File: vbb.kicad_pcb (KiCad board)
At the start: 2 copper layers, 24 parts, among them CON1 BARREL_JACK, J1 Screw_Terminal_1x02, P1 CONN_02X01, P3 CONN_02X04, P4 USB_B, P5 USB_B, P6 USB_B, P7 USB_A

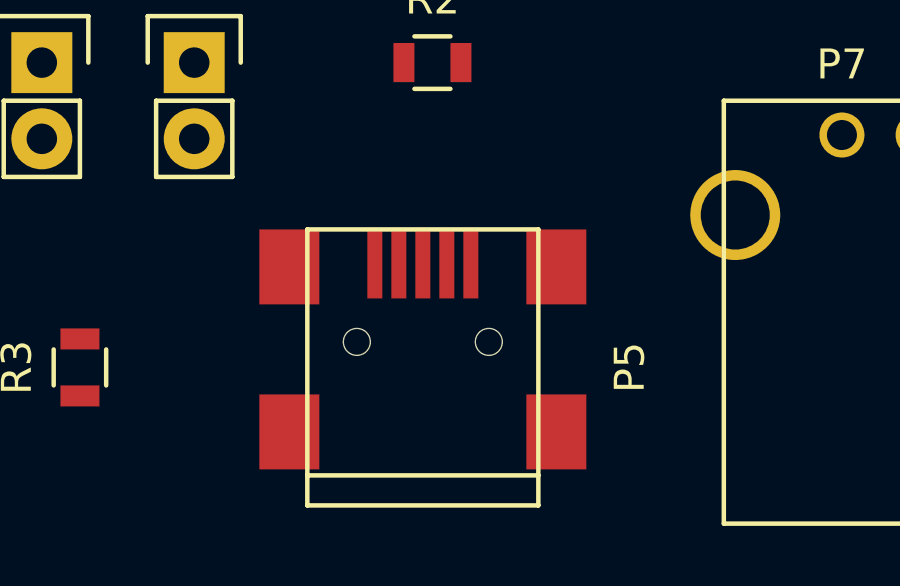
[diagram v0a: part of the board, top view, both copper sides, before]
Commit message: Replaced old surface mount USB Mini with through hole Omron Mini-USB B through hole XM7D-0512
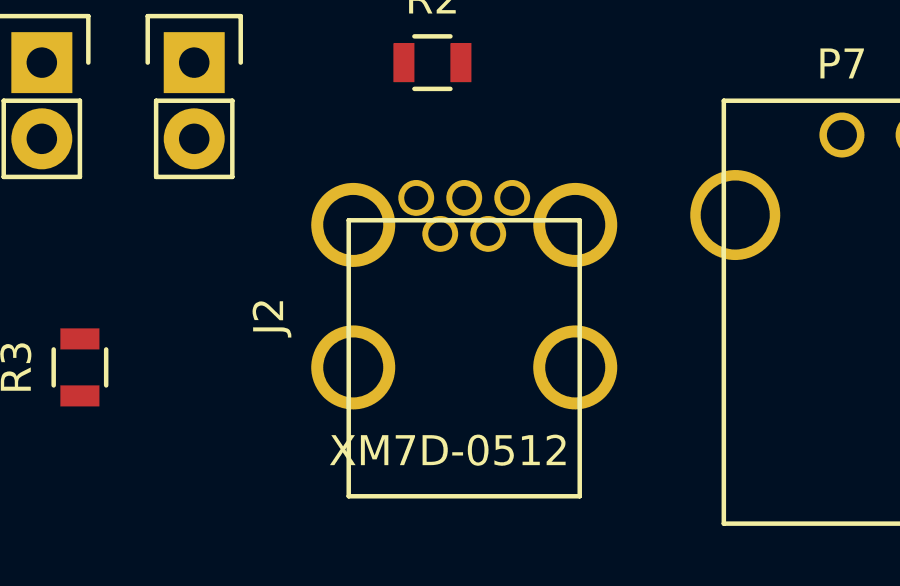
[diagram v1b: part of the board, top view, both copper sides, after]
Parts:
- removed P5: USB_B, Connect:USB_Mini-B
- added J2: XM7D-0512, Omron:XM7D-0512, F.Cu at (127.1, 116.1)

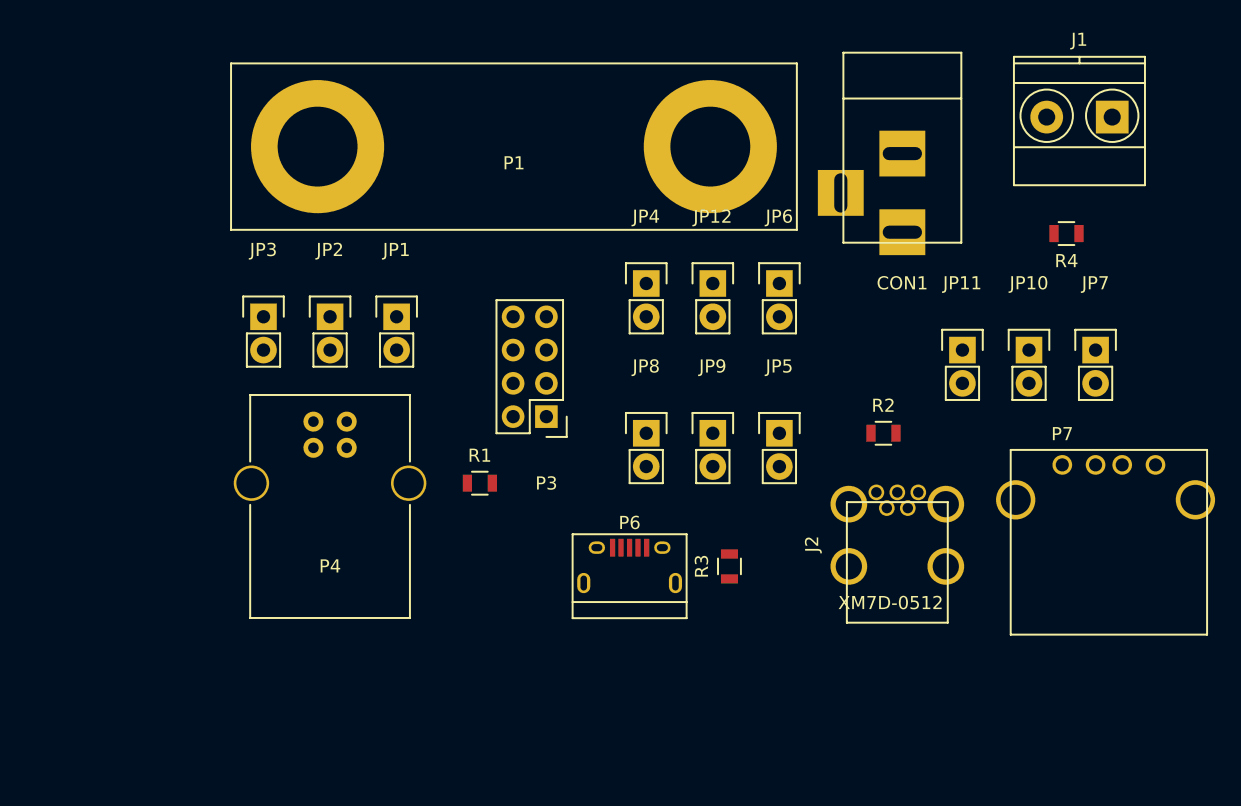
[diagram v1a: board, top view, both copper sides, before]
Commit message: Combined separate jumpers into a 2x03 connector As a result, board now fits the 50mmx50mm size group.
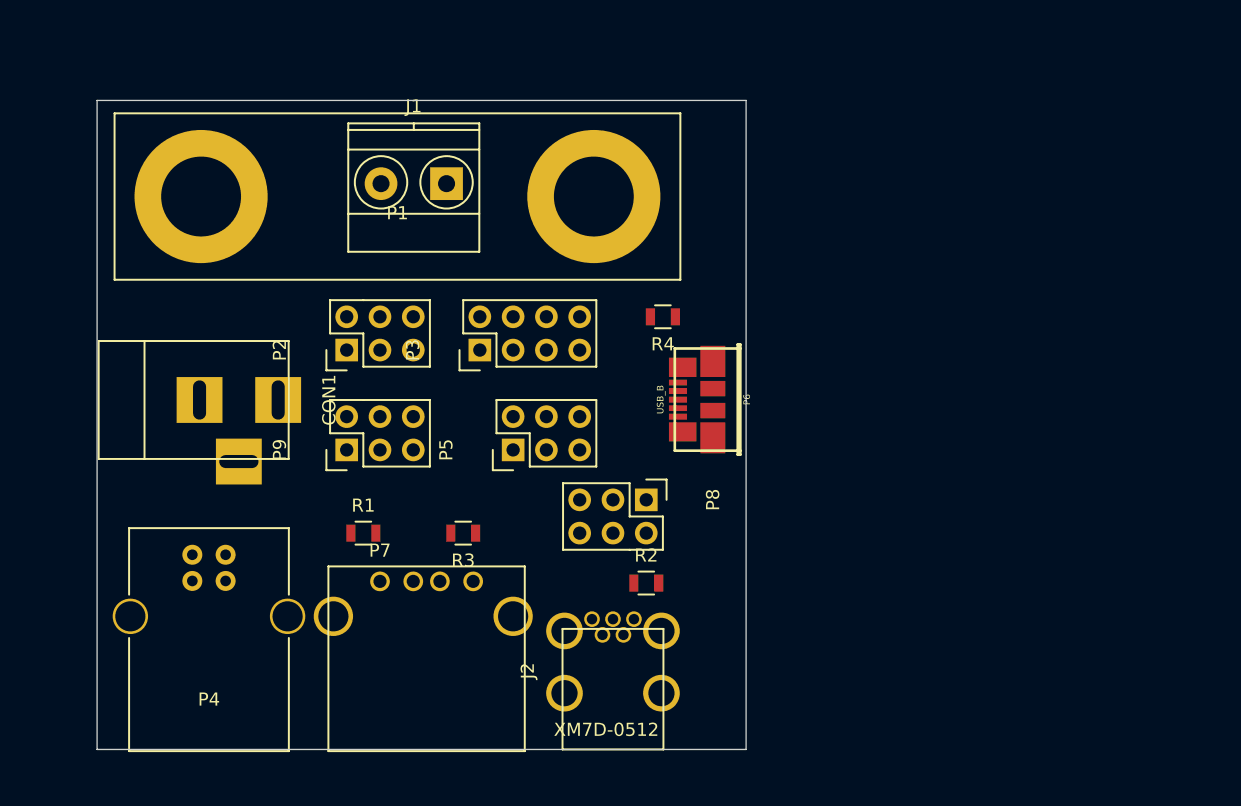
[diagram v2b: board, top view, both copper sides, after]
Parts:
- removed JP1, JP10, JP11, JP12, JP2, JP3, JP4, JP5, JP6, JP7, JP8, JP9: JUMPER_NO_Small, Pin_Headers:Pin_Header_Straight_1x02
- added P2: CONN_02X03, Pin_Headers:Pin_Header_Straight_2x03, F.Cu at (85.1, 95.2)
- added P5: CONN_02X03, Pin_Headers:Pin_Header_Straight_2x03, F.Cu at (97.8, 102.9)
- added P8: CONN_02X03, Pin_Headers:Pin_Header_Straight_2x03, F.Cu at (108.0, 106.7)
- added P9: CONN_02X03, Pin_Headers:Pin_Header_Straight_2x03, F.Cu at (85.1, 102.9)
- P6: footprint Connect:USB_Micro-B -> w_conn_pc:conn_usb_B_micro_smd
- moved CON1 57.1 mm to (73.7, 99.1), turned to 0 degrees
- moved P7 52.8 mm to (87.6, 112.9)
- moved J1 51.1 mm to (92.7, 82.5)
- moved R4 31.4 mm to (109.2, 92.7)
- moved J2 23.8 mm to (105.4, 125.7)
- moved R2 21.4 mm to (108.0, 113.0)
- moved R3 20.5 mm to (94.0, 109.2), turned to 180 degrees
- moved P6 14.3 mm to (113.0, 99.0), turned to 90 degrees
- moved P4 13.7 mm to (75.8, 110.9)
- moved P1 9.67 mm to (89.0, 83.5)
- moved R1 9.67 mm to (86.4, 109.2)
- moved P3 7.18 mm to (95.2, 95.2), turned to 90 degrees
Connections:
- P1 pad 2: /GND -> Net-(P1-Pad2)
- P3 pad 1: /GND -> Net-(P1-Pad2)
- P3 pad 3: /GND -> Net-(P1-Pad2)
- P3 pad 5: /GND -> Net-(P1-Pad2)
- P3 pad 7: /GND -> Net-(P1-Pad2)
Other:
- board outline added: 49.5 x 49.5 mm

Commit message: First pass through TopoR
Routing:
- net /GND: track 0.00 -> 112.6 mm
- net /VCC: track 0.00 -> 82.2 mm
- net Net-(P7-Pad5): track 0.00 -> 44.6 mm
- net Net-(P2-Pad3): track 0.00 -> 28.6 mm
- net Net-(J2-Pad2): track 0.00 -> 28.2 mm
- net Net-(P2-Pad6): track 0.00 -> 26.9 mm
- net Net-(P2-Pad5): track 0.00 -> 25.2 mm
- net Net-(P6-Pad5): track 0.00 -> 25.0 mm
- net Net-(P2-Pad2): track 0.00 -> 24.1 mm
- net Net-(P2-Pad4): track 0.00 -> 23.6 mm
- net Net-(P4-Pad5): track 0.00 -> 21.3 mm
- net Net-(J2-Pad0): track 0.00 -> 20.6 mm
- net Net-(P1-Pad2): track 0.00 -> 19.7 mm
- net Net-(J2-Pad3): track 0.00 -> 16.9 mm
- net Net-(J2-Pad1): track 0.00 -> 16.8 mm
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
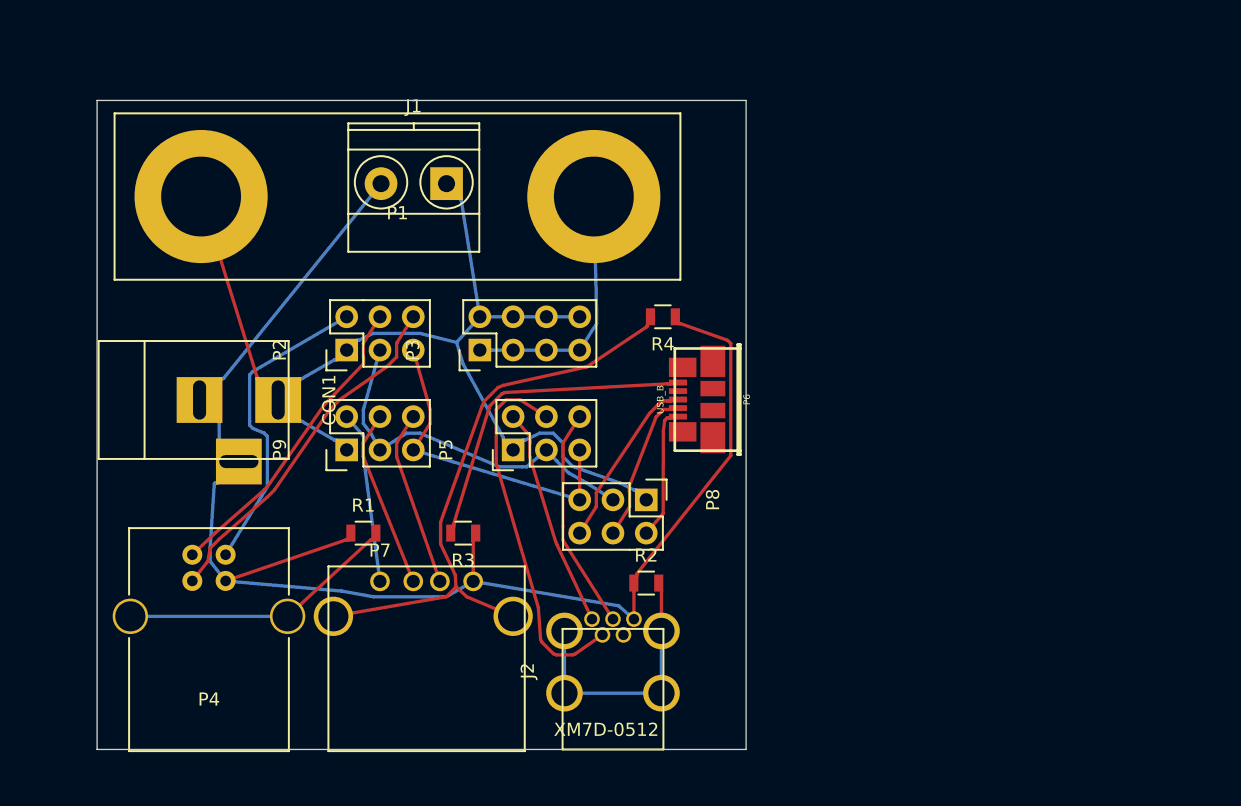
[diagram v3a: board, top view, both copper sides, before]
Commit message: Files should be ready: Copper pours on both sides Added jumpers for current measurement Added silkscreen text VCC/GNC tracks are twice as wide.
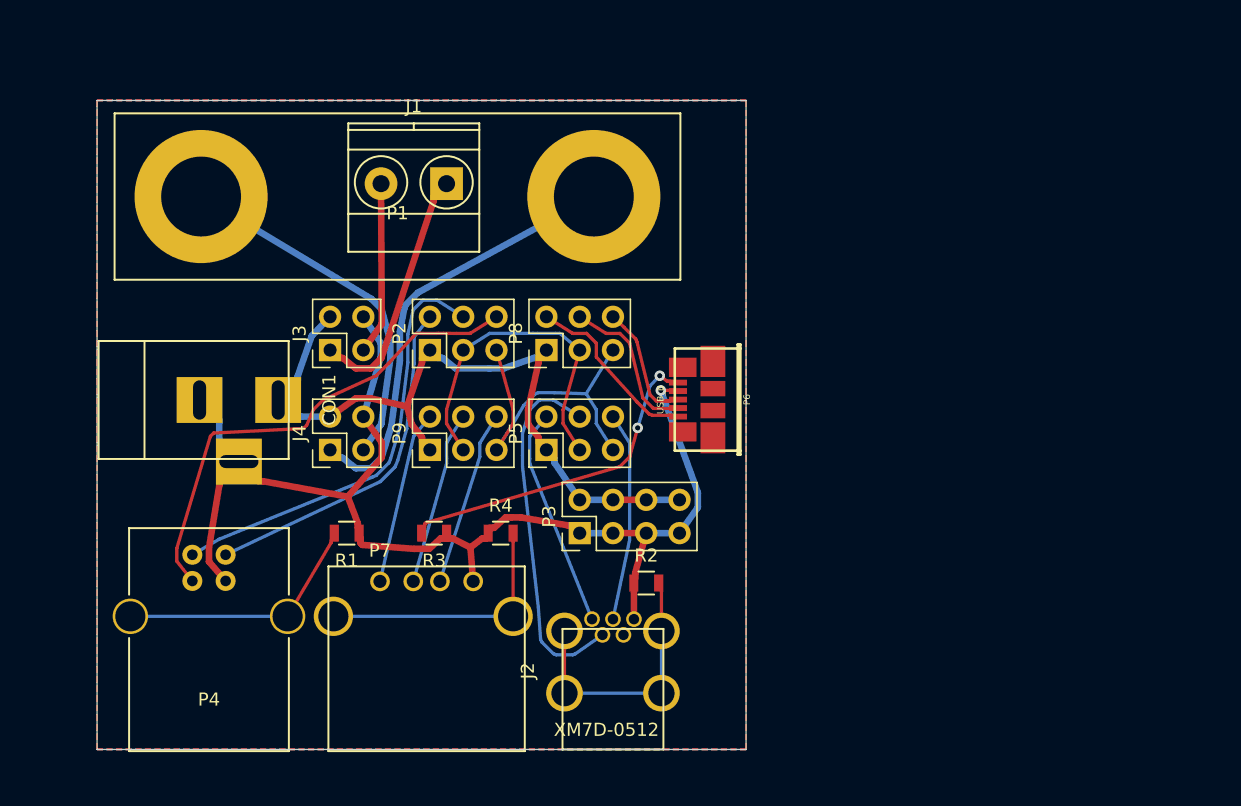
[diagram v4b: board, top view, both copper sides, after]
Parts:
- added J3: CONN_02X02, Pin_Headers:Pin_Header_Straight_2x02_Pitch2.54mm, F.Cu at (83.8, 95.2)
- added J4: CONN_02X02, Pin_Headers:Pin_Header_Straight_2x02_Pitch2.54mm, F.Cu at (83.8, 102.9)
- P2, P5, P8, P9: footprint Pin_Headers:Pin_Header_Straight_2x03 -> Pin_Headers:Pin_Header_Straight_2x03_Pitch2.54mm
- P3: footprint Pin_Headers:Pin_Header_Straight_2x04 -> Pin_Headers:Pin_Header_Straight_2x04_Pitch2.54mm
- moved R4 20.6 mm to (96.8, 109.2), turned to 0 degrees
- moved P3 15.9 mm to (102.9, 109.2)
- moved P8 13.7 mm to (100.3, 95.2), turned to 90 degrees
- moved P2 6.35 mm to (91.4, 95.2)
- moved P9 6.35 mm to (91.4, 102.9)
- moved P5 2.54 mm to (100.3, 102.9)
- moved R3 2.22 mm to (91.8, 109.2)
- moved R1 1.27 mm to (85.1, 109.2), turned to 180 degrees
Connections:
- J1 pad 1: /VCC -> /VCC2
- J1 pad 2: /GND -> /GND2
- P1 pad 1: /VCC -> /GND1
- P1 pad 2: Net-(P1-Pad2) -> /VCC1
- P3 pad 1: Net-(P1-Pad2) -> /GND
- P3 pad 3: Net-(P1-Pad2) -> /GND
- P3 pad 5: Net-(P1-Pad2) -> /GND
- P3 pad 7: Net-(P1-Pad2) -> /GND
- P6 pad 4: Net-(P6-Pad4) -> /GND
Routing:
- net /VCC1: track 0.00 -> 33.3 mm
- net /GND1: track 0.00 -> 27.6 mm
- net /VCC: track 82.2 -> 57.7 mm
- net Net-(P7-Pad5): track 44.6 -> 20.1 mm
- net Net-(P1-Pad2): track 19.7 -> 0.00 mm
- net /VCC2: track 0.00 -> 19.1 mm
- net /GND: track 112.6 -> 94.1 mm, vias 0 -> 1
- net /GND2: track 0.00 -> 13.1 mm
- net Net-(P2-Pad6): track 26.9 -> 37.1 mm
- net Net-(P2-Pad4): track 23.6 -> 33.0 mm
- net Net-(P6-Pad3): track 13.3 -> 9.17 mm
- net Net-(P6-Pad1): track 10.2 -> 13.7 mm
- net Net-(P2-Pad2): track 24.1 -> 26.7 mm
- net Net-(P2-Pad3): track 28.6 -> 26.0 mm
- net Net-(P4-Pad5): track 21.3 -> 19.3 mm
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- added copper zone on B.Cu, net /GND
- added copper zone on F.Cu, net /GND
- added copper zone on B.Cu, net /VCC
- added copper zone on F.Cu, net /VCC
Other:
- net class GND added: clearance 0.2, trace_width 0.5, via_dia 0.8, via_drill 0.4
- net class VCC added: clearance 0.2, trace_width 0.5, via_dia 0.8, via_drill 0.4
- board text added: "VCC Breakout Board"
- board text added: "© 2017 Udi Finkelstein https://github.com/udif/vbb"

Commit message: Fixes DRC by changing track-to-track clearance to 0.18mm and by deleting redundant multiple copper pours.
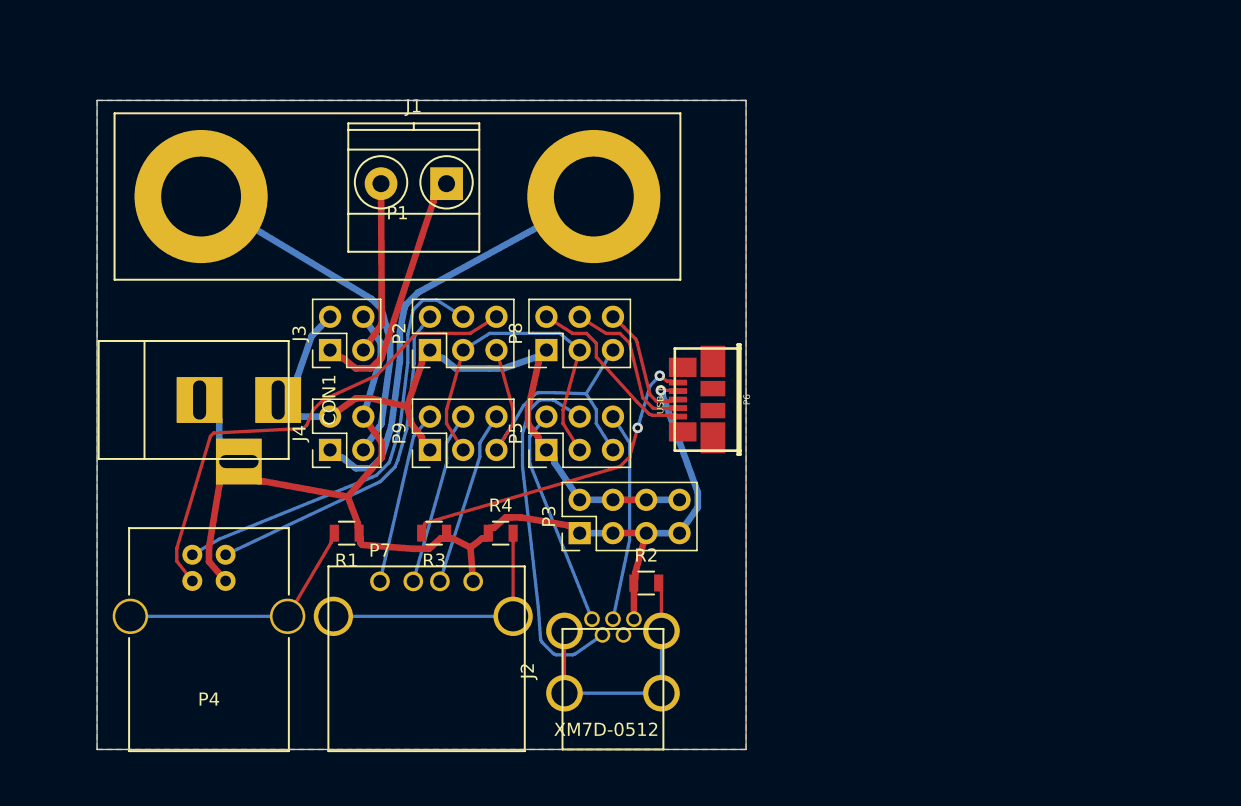
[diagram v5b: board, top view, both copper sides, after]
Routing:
- removed copper zone on B.Cu, net /GND
- removed copper zone on F.Cu, net /VCC
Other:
- net class Default: clearance 0.2 -> 0.18
- rule trace_clearance: 0.2 -> 0.18
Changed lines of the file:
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@@
   (layers
     (0 F.Cu signal)
-    (31 B.Cu signal hide)
+    (31 B.Cu signal)
     (32 B.Adhes user)
     (33 F.Adhes user)
@@
   (setup
     (last_trace_width 0.25)
-    (trace_clearance 0.2)
+    (trace_clearance 0.18)
     (zone_clearance 0.508)
     (zone_45_only no)
@@
     (pad_to_mask_clearance 0)
     (aux_axis_origin 0 0)
-    (visible_elements 7FFFFFFF)
+    (visible_elements 7FFFEFFF)
     (pcbplotparams
-      (layerselection 0x00030_ffffffff)
+      (layerselection 0x000fc_ffffffff)
       (usegerberextensions false)
       (excludeedgelayer true)
@@
   (net 25 /VCC1)
   (net_class Default "This is the default net class."
-    (clearance 0.2)
+    (clearance 0.18)
     (trace_width 0.25)
     (via_dia 0.8)
@@
   (segment (start 90.5271 90.8649) (end 89.5949 91.7971) (width 0.5) (layer B.Cu) (net 25))
   (segment (start 103.9498 83.534) (end 90.5271 90.8649) (width 0.5) (layer B.Cu) (net 25))
-  (zone (net 1) (net_name /GND) (layer B.Cu) (hatch edge 0.508)
-    (connect_pads (clearance 0.508))
-    (min_thickness 0.254)
-    (fill (arc_segments 16) (thermal_gap 0.508) (thermal_bridge_width 0.508))
-    (polygon
-      (pts
-        (xy 115.57 125.73) (xy 66.04 125.73) (xy 66.04 76.2) (xy 115.57 76.2)
-      )
-    )
-  )
-  (zone (net 1) (net_name /GND) (layer B.Cu) (hatch edge 0.508)
-    (connect_pads (clearance 0.508))
-    (min_thickness 0.254)
-    (fill (arc_segments 16) (thermal_gap 0.508) (thermal_bridge_width 0.508))
-    (polygon
-      (pts
-        (xy 66.04 76.2) (xy 115.57 76.2) (xy 115.57 125.73) (xy 66.04 125.73)
-      )
-    )
-  )
-  (zone (net 2) (net_name /VCC) (layer F.Cu) (hatch edge 0.508)
-    (connect_pads (clearance 0.508))
-    (min_thickness 0.254)
-    (fill (arc_segments 16) (thermal_gap 0.508) (thermal_bridge_width 0.508))
-    (polygon
-      (pts
-        (xy 66.04 76.2) (xy 115.57 76.2) (xy 115.57 125.73) (xy 66.04 125.73)
-      )
-    )
-  )
   (zone (net 1) (net_name /GND) (layer F.Cu) (hatch edge 0.508)
     (connect_pads (clearance 0.508))
-    (min_thickness 0.254)
-    (fill (arc_segments 16) (thermal_gap 0.508) (thermal_bridge_width 0.508))
-    (polygon
-      (pts
-        (xy 66.04 76.2) (xy 115.57 76.2) (xy 115.57 125.73) (xy 66.04 125.73)
-      )
-    )
-  )
-  (zone (net 2) (net_name /VCC) (layer B.Cu) (hatch edge 0.508)
-    (connect_pads (clearance 0.508))
-    (min_thickness 0.254)
-    (fill (arc_segments 16) (thermal_gap 0.508) (thermal_bridge_width 0.508))
-    (polygon
-      (pts
-        (xy 66.04 76.2) (xy 115.57 76.2) (xy 115.57 125.73) (xy 66.04 125.73)
-      )
-    )
-  )
-  (zone (net 2) (net_name /VCC) (layer B.Cu) (hatch edge 0.508)
-    (connect_pads (clearance 0.508))
-    (min_thickness 0.254)
-    (fill (arc_segments 16) (thermal_gap 0.508) (thermal_bridge_width 0.508))
-    (polygon
-      (pts
-        (xy 66.04 76.2) (xy 115.57 76.2) (xy 115.57 125.73) (xy 66.04 125.73)
-      )
-    )
-  )
-  (zone (net 2) (net_name /VCC) (layer B.Cu) (hatch edge 0.508)
-    (connect_pads (clearance 0.508))
-    (min_thickness 0.254)
-    (fill (arc_segments 16) (thermal_gap 0.508) (thermal_bridge_width 0.508))
-    (polygon
-      (pts
-        (xy 66.04 76.2) (xy 115.57 76.2) (xy 115.57 125.73) (xy 66.04 125.73)
-      )
-    )
-  )
-  (zone (net 1) (net_name /GND) (layer F.Cu) (hatch edge 0.508)
-    (connect_pads (clearance 0.508))
-    (min_thickness 0.254)
-    (fill (arc_segments 16) (thermal_gap 0.508) (thermal_bridge_width 0.508))
-    (polygon
-      (pts
-        (xy 66.04 76.2) (xy 115.57 76.2) (xy 115.57 125.73) (xy 66.04 125.73)
-      )
-    )
-  )
-  (zone (net 2) (net_name /VCC) (layer B.Cu) (hatch edge 0.508)
-    (connect_pads (clearance 0.508))
-    (min_thickness 0.254)
-    (fill (arc_segments 16) (thermal_gap 0.508) (thermal_bridge_width 0.508))
-    (polygon
-      (pts
-        (xy 66.04 76.2) (xy 115.57 76.2) (xy 115.57 125.73) (xy 66.04 125.73)
-      )
-    )
-  )
-  (zone (net 1) (net_name /GND) (layer F.Cu) (hatch edge 0.508)
-    (connect_pads (clearance 0.508))
